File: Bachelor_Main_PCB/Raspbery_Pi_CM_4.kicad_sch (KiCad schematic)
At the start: 19 parts, among them J21 M20-9990245, Q12 NX3008NBKW, Q13 NX3008NBKW, Q2 SSM3J358R,LF, U1 SC0683, X1 DF40HC_3.0_-100DS-0.4V_58, X2 DF40HC_3.0_-100DS-0.4V_58

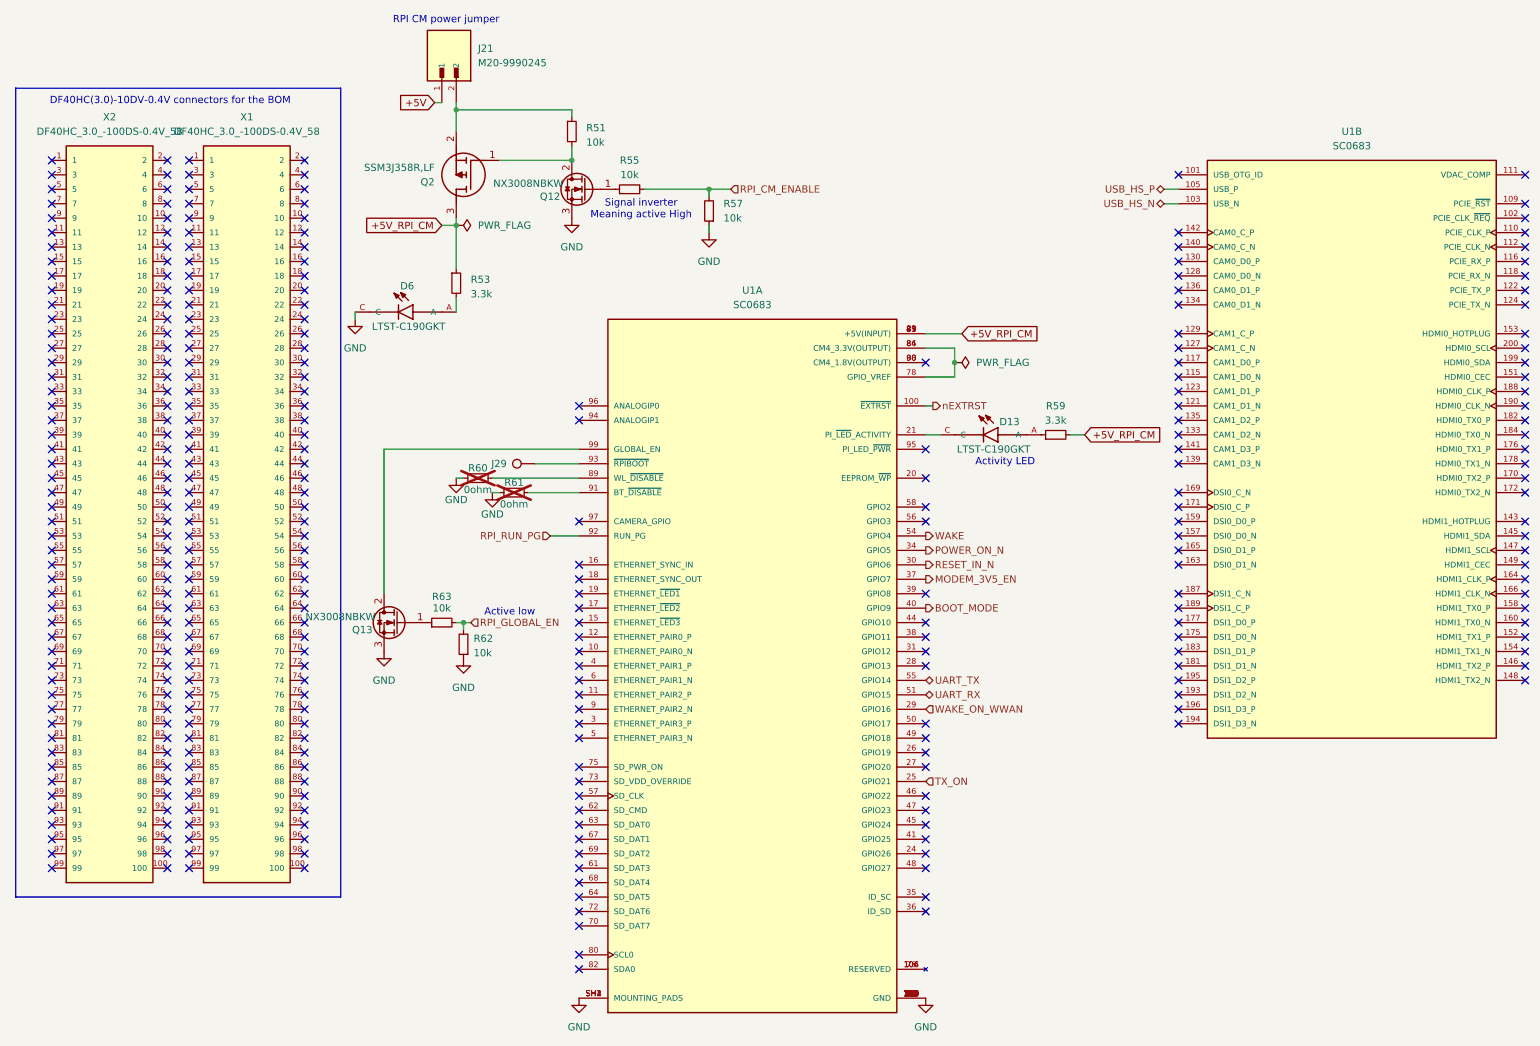
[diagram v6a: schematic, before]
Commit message: Imported components from schematic to PCB and Reanotat all designators
THis means every designator is now different and the references made prior no longer applies
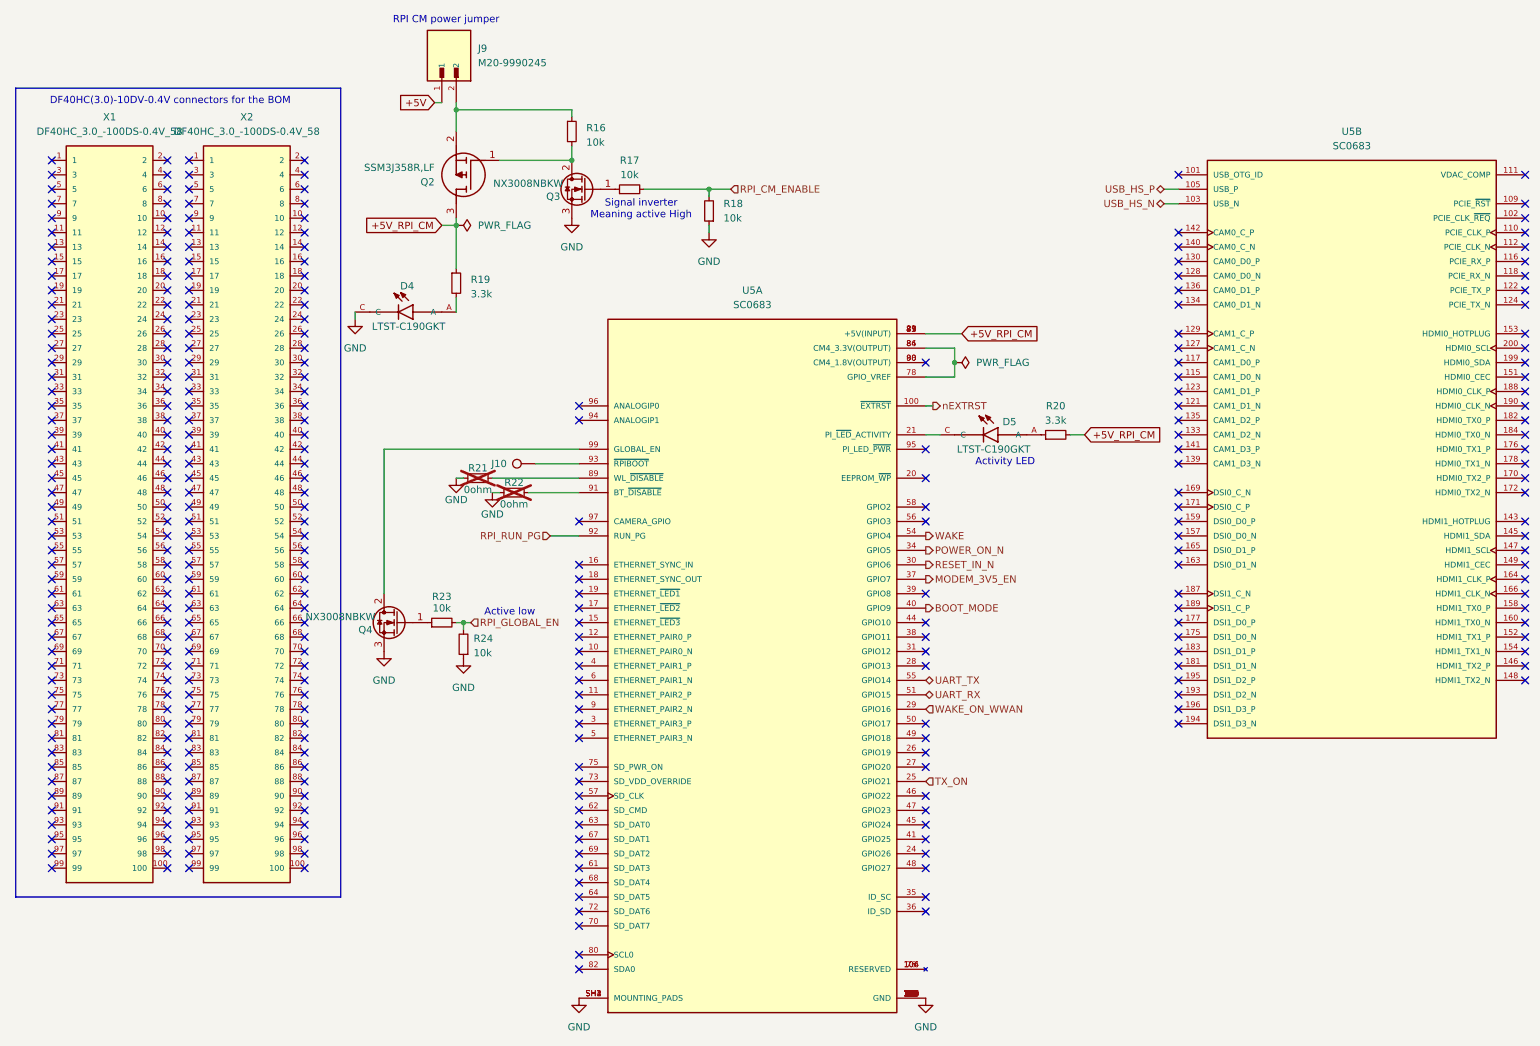
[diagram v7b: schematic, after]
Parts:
- renumbered D6 to D4, D13 to D5, J29 to J10, J21 to J9, Q12 to Q3, Q13 to Q4, R51 to R16, R55 to R17, R57 to R18, R53 to R19, R59 to R20, R60 to R21, R61 to R22, R63 to R23, R62 to R24, U1 to U5, X2 to X1, X1 to X2

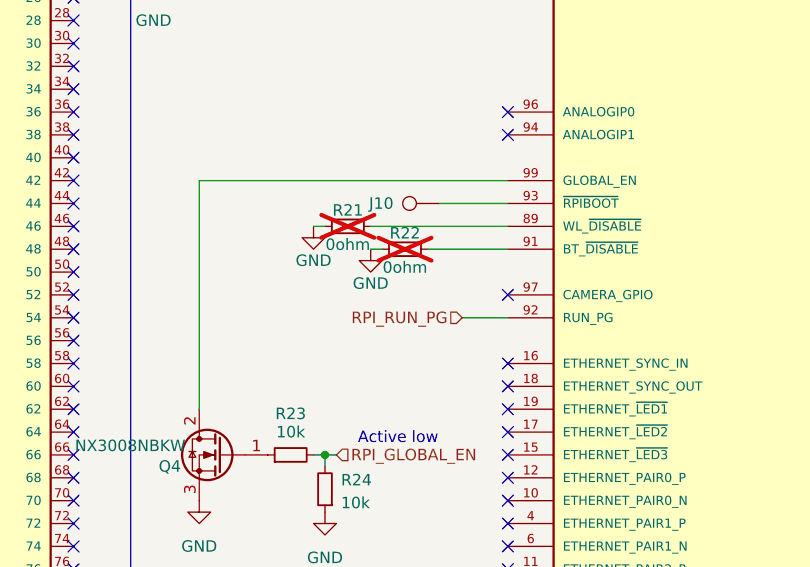
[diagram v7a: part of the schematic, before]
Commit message: Changed V_IN on adc mcu sense pin to V_VIN_MEAS
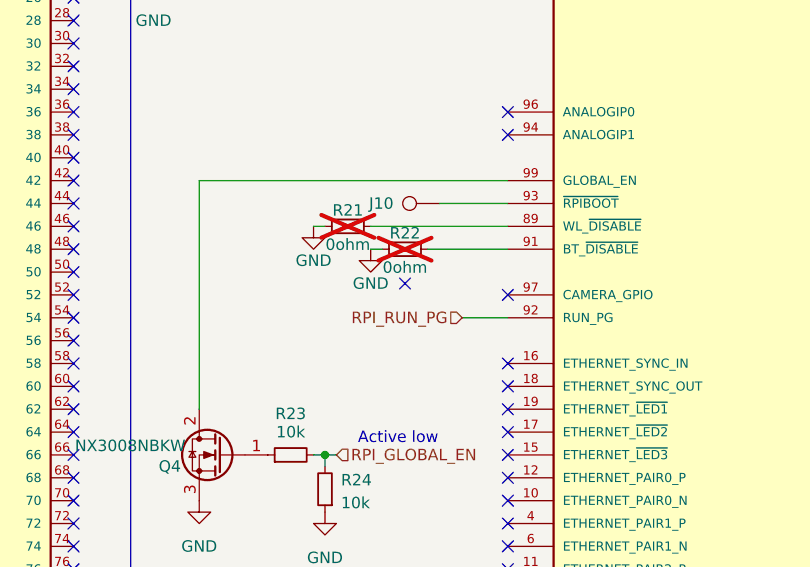
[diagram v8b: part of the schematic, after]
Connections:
- no-connect marks 318 -> 319
